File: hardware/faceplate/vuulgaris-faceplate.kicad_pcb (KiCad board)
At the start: 4 copper layers, 298.3 x 137.8 mm, 1 part, among them J1 2x5 SMD box header -- PLACEHO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

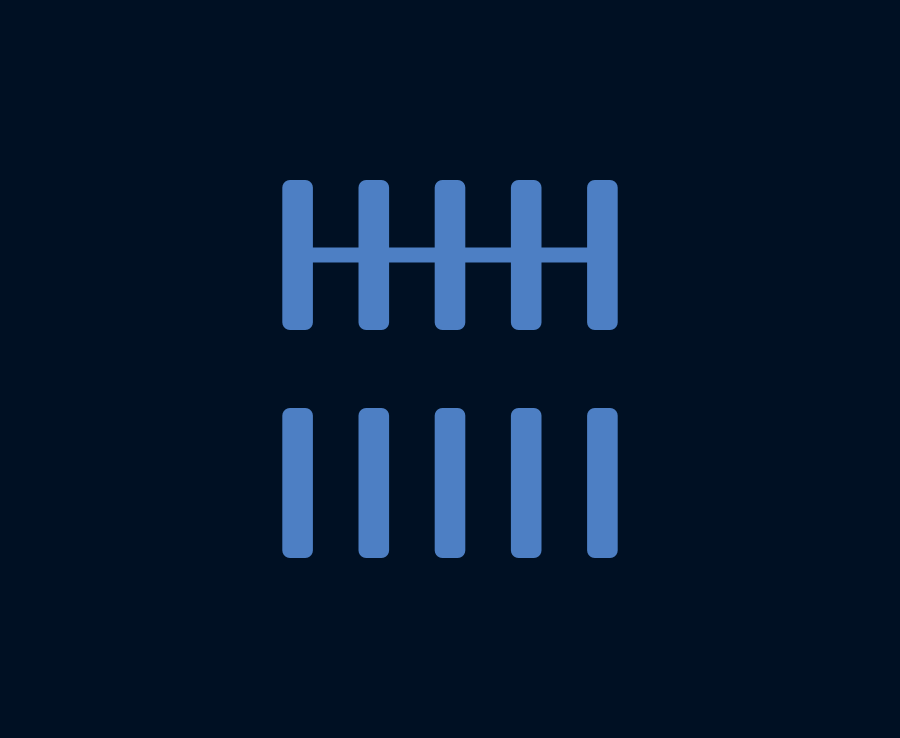
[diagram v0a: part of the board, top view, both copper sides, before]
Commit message: faceplate: J1 is the hanxia HX JN2.54-2x5P TP H8.9 (C41376028)
The cable header's placeholder (KiCad's generic SMD box header) is replaced by
a real part. It is Extended: JLC's Basic filter returns no SMD 2x5 box header
at all. Of the SMD ones, this has the most JLC stock (4715) and a drawing with
a recommended land pattern; the runner-up, XFCN BH254VS-10P (C492446), is
10.5mm tall against a 10mm gap. This one seats at 9.60mm.

New footprint IDC-SMD_10P-P2.54_C41376028 in the shared library, from hanxia's
drawing (datasheets/hanxia-HX-JN2.54-2x5P-TP-H8.9.pdf, now in
fetch-datasheets.sh), read at 6x: pads 1.02 x 4.65 on 2.54mm pitch, 11.50
overall (row centres +-3.425); body 20.30 x 8.90; leg tips 10.20 across; key
slot 4.50 wide. Fab carries the body and the leg tips, which is what
panelcheck measures against the cutout. The drawing marks pin 1 only by a
triangle on the key wall, so pin 1 is on the key-side row at that end -- the
same convention as KiCad's DIN 41651 footprint and main-board J12. Still to be
confirmed with a real ribbon before ordering (README section 5).

Board: J1 swapped by a one-off pcbnew script using mkboard.py's rule (pad
centroid on the cutout centre, pad 1 the way J12's lies, on B.Cu) and its
four GND row joins redrawn for the new pads. Diffed against HEAD: J1 and
those four segments are the only changes; the centroid is where it was.

Checked: netcheck 10/10, 0 unintended; boardcheck 0/0/0; DRC 0 errors, 0
warnings (the stock footprint's warning is gone); panelcheck 6 OK -- body and
legs 20.40 x 10.30 in the 24 x 12 cutout, tightest side 0.85mm.
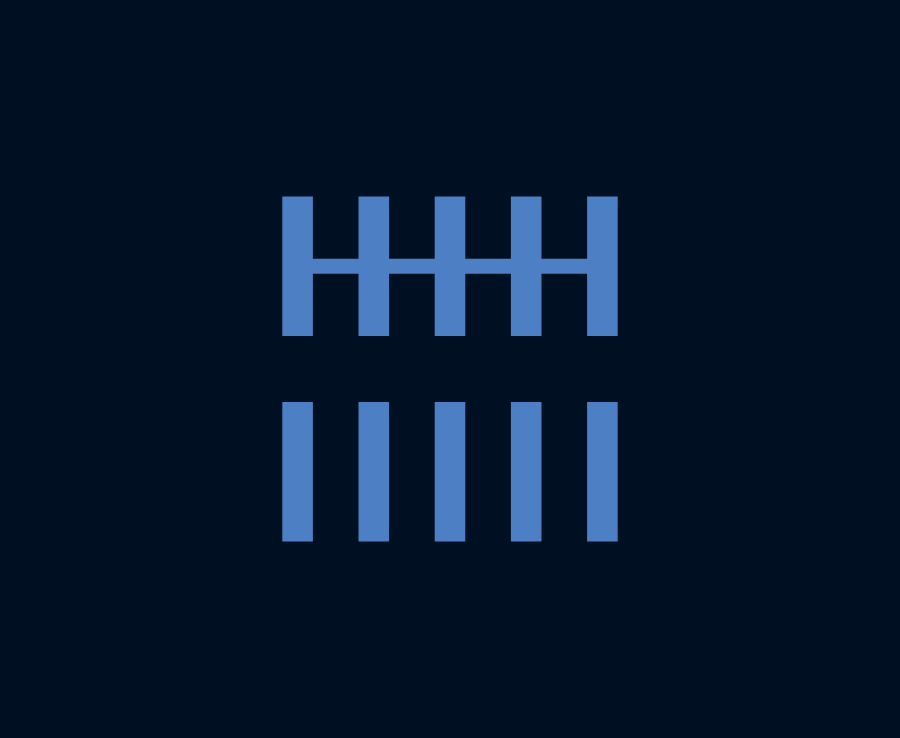
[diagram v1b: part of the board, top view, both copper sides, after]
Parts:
- J1: value 2x5 SMD box header -- PLACEHOLDER, part not chosen -> HX JN2.54-2x5P TP H8.9; footprint Connector_IDC:IDC-Header_2x05_P2.54mm_Vertical_SMD -> vuulgaris:IDC-SMD_10P-P2.54_C41376028
- turned J1 to 180 degrees

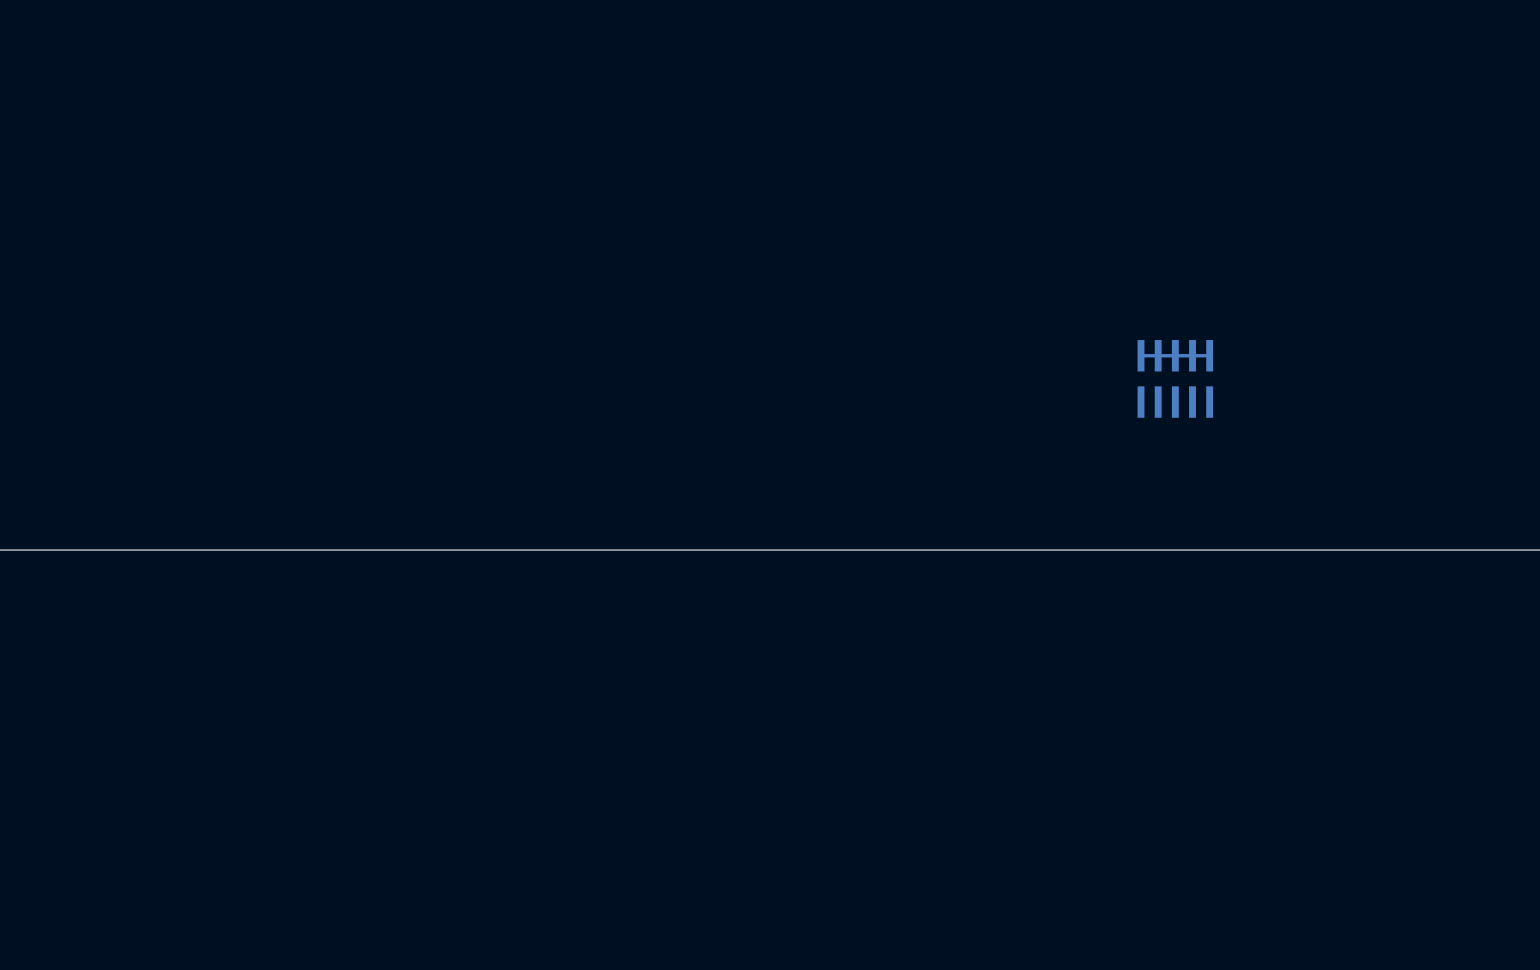
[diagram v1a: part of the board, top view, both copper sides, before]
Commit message: faceplate: pad copper on the board, one open via per bar
The generator drew every bar as its own island -- 800 of them, joined to
nothing. TI's SLAA891 elements are single bodies, so the cross-check turned
into a connectivity decision: one via per bar (Dylan's call), open, not
filled or capped, and open on the back so nothing traps plating chemistry.

Generator: copper() places a 0.3/0.5 via 0.5mm in from each bar's outer
edge; bars too short for one (the 0.197mm slivers, and five thin RX0 bars
behind J1 on pad 4) are bridged along the pad edge to a same-net bar that
has one. Vias walk inward to clear J1's pad rows on the back. Hole and
bridge copper go into the area compensation; --check now measures all four
pads with both counted: 0.00mm worst error (0.72mm and 2.02mm without,
watched failing). 763 vias, 37 bridges.

design/mkpads.py writes SCRUB_PAD_216x10_P1..P4 (bars as roundrect pads
numbered by E's pins, one F.Mask opening, B.Mask open at each via, no
paste, allow_soldermask_bridges) and places E1-E4 and the vias via pcbnew.
panelcheck checks the board's pads and vias against copper() to 1um, and
the generator's keepouts against J1's real pads; both watched failing.

drc.py --unrouted: the board is placed for hand-routing, so unconnected
items are the ratsnest; every other error still fails (watched on a
planted clearance violation). Bare drc.py remains the fab check.

Checked: generator --check all pass, placement file unchanged;
mksch/netcheck 145/145; boardcheck parity 0, clearance 0; DRC --unrouted
0 errors; panelcheck 9 OK; main board DRC 0 errors, place.py all 24.
The other 50 footprints came in from the schematic and are parked off
the outline until the next commit.
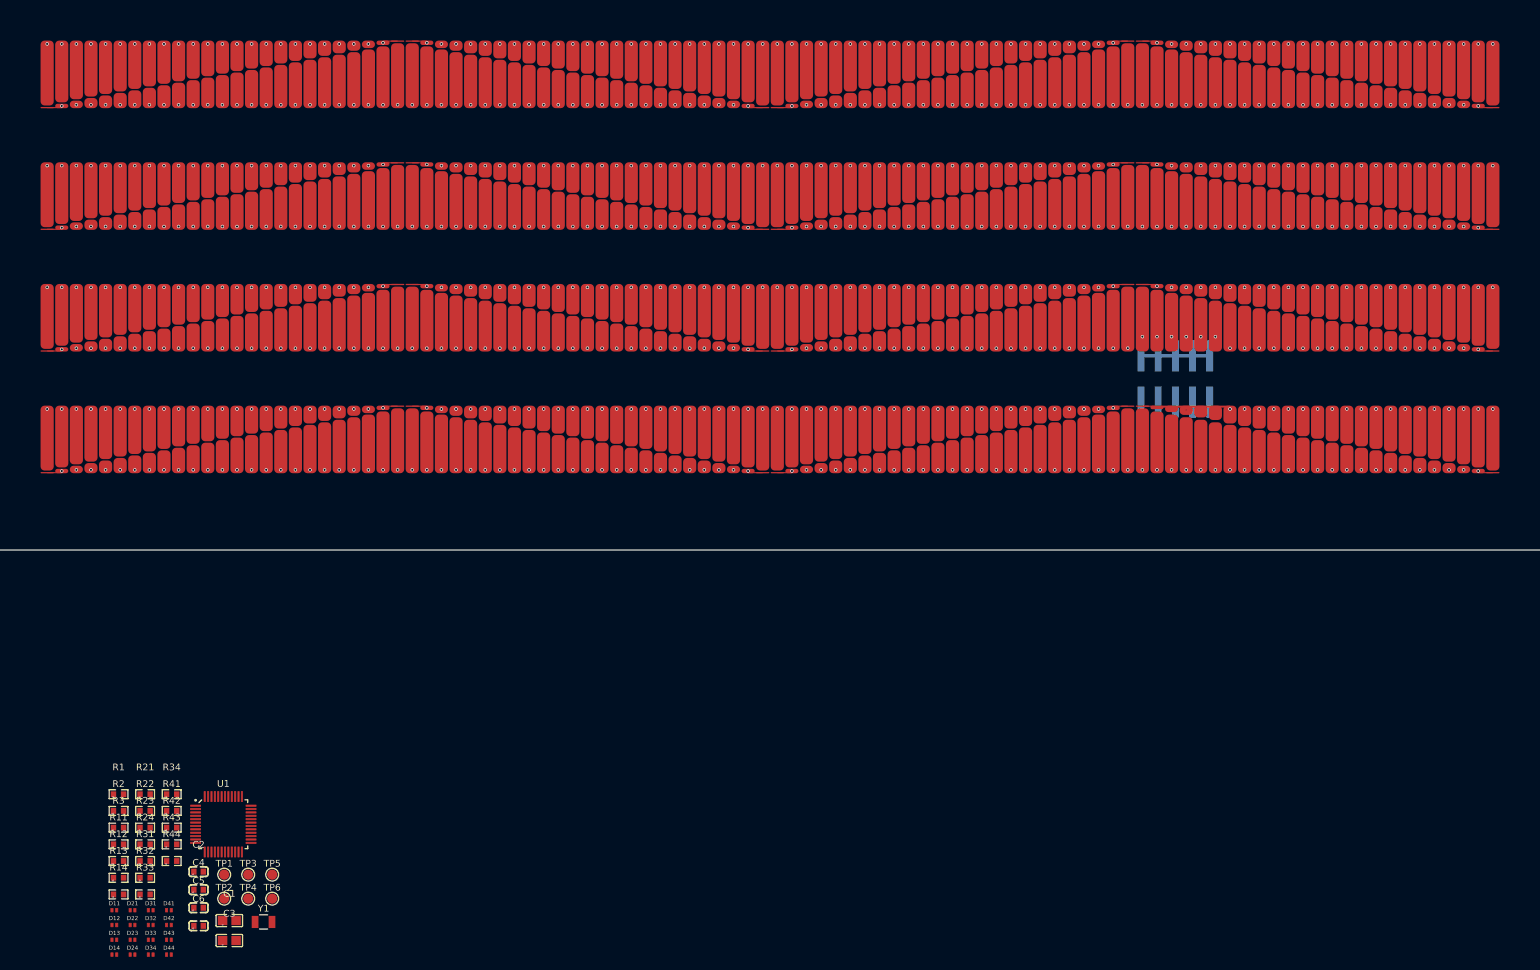
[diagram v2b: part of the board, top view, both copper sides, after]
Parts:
- added C1: 10uF, vuulgaris:C0805, F.Cu at (189.1, 242.6)
- added C2: 100nF, vuulgaris:C0603, F.Cu at (184.5, 235.4)
- added C3: 1uF, vuulgaris:C0805, F.Cu at (189.1, 245.6)
- added C4: 1nF C0G, vuulgaris:C0603, F.Cu at (184.5, 238.1)
- added C5: 22pF C0G, vuulgaris:C0603, F.Cu at (184.5, 240.7)
- added C6: 22pF C0G, vuulgaris:C0603, F.Cu at (184.5, 243.4)
- added D11: TPD1E10B06DPYR, vuulgaris:X1SON-2_DPY0002A, F.Cu at (172.1, 241.1)
- added D12: TPD1E10B06DPYR, vuulgaris:X1SON-2_DPY0002A, F.Cu at (172.1, 243.3)
- added D13: TPD1E10B06DPYR, vuulgaris:X1SON-2_DPY0002A, F.Cu at (172.1, 245.5)
- added D14: TPD1E10B06DPYR, vuulgaris:X1SON-2_DPY0002A, F.Cu at (172.1, 247.7)
- added D21: TPD1E10B06DPYR, vuulgaris:X1SON-2_DPY0002A, F.Cu at (174.7, 241.1)
- added D22: TPD1E10B06DPYR, vuulgaris:X1SON-2_DPY0002A, F.Cu at (174.7, 243.3)
- added D23: TPD1E10B06DPYR, vuulgaris:X1SON-2_DPY0002A, F.Cu at (174.7, 245.5)
- added D24: TPD1E10B06DPYR, vuulgaris:X1SON-2_DPY0002A, F.Cu at (174.7, 247.7)
- added D31: TPD1E10B06DPYR, vuulgaris:X1SON-2_DPY0002A, F.Cu at (177.4, 241.1)
- added D32: TPD1E10B06DPYR, vuulgaris:X1SON-2_DPY0002A, F.Cu at (177.4, 243.3)
- added D33: TPD1E10B06DPYR, vuulgaris:X1SON-2_DPY0002A, F.Cu at (177.4, 245.5)
- added D34: TPD1E10B06DPYR, vuulgaris:X1SON-2_DPY0002A, F.Cu at (177.4, 247.7)
- added D41: TPD1E10B06DPYR, vuulgaris:X1SON-2_DPY0002A, F.Cu at (180.1, 241.1)
- added D42: TPD1E10B06DPYR, vuulgaris:X1SON-2_DPY0002A, F.Cu at (180.1, 243.3)
- added D43: TPD1E10B06DPYR, vuulgaris:X1SON-2_DPY0002A, F.Cu at (180.1, 245.5)
- added D44: TPD1E10B06DPYR, vuulgaris:X1SON-2_DPY0002A, F.Cu at (180.1, 247.7)
- added E1: SCRUB_PAD_216x10_P1, vuulgaris:SCRUB_PAD_216x10_P1, F.Cu at (269.1, 117.5)
- added E2: SCRUB_PAD_216x10_P2, vuulgaris:SCRUB_PAD_216x10_P2, F.Cu at (269.1, 135.5)
- added E3: SCRUB_PAD_216x10_P3, vuulgaris:SCRUB_PAD_216x10_P3, F.Cu at (269.1, 153.5)
- added E4: SCRUB_PAD_216x10_P4, vuulgaris:SCRUB_PAD_216x10_P4, F.Cu at (269.1, 171.5)
- added R1: 47k, vuulgaris:R0603, F.Cu at (172.7, 223.9)
- added R11: 470, vuulgaris:R0603, F.Cu at (172.7, 231.3)
- added R12: 470, vuulgaris:R0603, F.Cu at (172.7, 233.8)
- added R13: 470, vuulgaris:R0603, F.Cu at (172.7, 236.3)
- added R14: 470, vuulgaris:R0603, F.Cu at (172.7, 238.8)
- added R2: 47k, vuulgaris:R0603, F.Cu at (172.7, 226.4)
- added R21: 470, vuulgaris:R0603, F.Cu at (176.6, 223.9)
- added R22: 470, vuulgaris:R0603, F.Cu at (176.6, 226.4)
- added R23: 470, vuulgaris:R0603, F.Cu at (176.6, 228.9)
- added R24: 470, vuulgaris:R0603, F.Cu at (176.6, 231.3)
- added R3: 47k, vuulgaris:R0603, F.Cu at (172.7, 228.9)
- added R31: 470, vuulgaris:R0603, F.Cu at (176.6, 233.8)
- added R32: 470, vuulgaris:R0603, F.Cu at (176.6, 236.3)
- added R33: 470, vuulgaris:R0603, F.Cu at (176.6, 238.8)
- added R34: 470, vuulgaris:R0603, F.Cu at (180.5, 223.9)
- added R41: 470, vuulgaris:R0603, F.Cu at (180.5, 226.4)
- added R42: 470, vuulgaris:R0603, F.Cu at (180.5, 228.9)
- added R43: 470, vuulgaris:R0603, F.Cu at (180.5, 231.3)
- added R44: 470, vuulgaris:R0603, F.Cu at (180.5, 233.8)
- added TP1: SBW TEST, vuulgaris:TestPoint_Pad_D1.5mm, F.Cu at (188.3, 235.8)
- added TP2: SBW RST, vuulgaris:TestPoint_Pad_D1.5mm, F.Cu at (188.3, 239.4)
- added TP3: SBW 3V3, vuulgaris:TestPoint_Pad_D1.5mm, F.Cu at (191.9, 235.8)
- added TP4: SBW GND, vuulgaris:TestPoint_Pad_D1.5mm, F.Cu at (191.9, 239.4)
- added TP5: TP UART TX, vuulgaris:TestPoint_Pad_D1.5mm, F.Cu at (195.4, 235.8)
- added TP6: TP UART RX, vuulgaris:TestPoint_Pad_D1.5mm, F.Cu at (195.4, 239.4)
- added U1: MSP430FR2675TPT, vuulgaris:LQFP-48_7x7mm_P0.5mm_PT0048A, F.Cu at (188.2, 228.4)
- added Y1: 32.768kHz FC-135 12.5pF, vuulgaris:XTAL-SMD_FC-135_3.2x1.5mm, F.Cu at (194.1, 242.8)
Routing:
- net /PAD4_RX3: vias 0 -> 48
- net /PAD4_RX2: vias 0 -> 48
- net /PAD4_RX1: vias 0 -> 48
- net /PAD4_RX0: vias 0 -> 43
- net /PAD3_RX3: vias 0 -> 48
- net /PAD3_RX2: vias 0 -> 48
- net /PAD3_RX1: vias 0 -> 48
- net /PAD3_RX0: vias 0 -> 48
- net /PAD2_RX3: vias 0 -> 48
- net /PAD2_RX2: vias 0 -> 48
- net /PAD2_RX1: vias 0 -> 48
- net /PAD2_RX0: vias 0 -> 48
- net /PAD1_RX3: vias 0 -> 48
- net /PAD1_RX2: vias 0 -> 48
- net /PAD1_RX1: vias 0 -> 48
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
